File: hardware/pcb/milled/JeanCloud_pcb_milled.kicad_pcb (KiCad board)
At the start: 2 copper layers, 65 x 49 mm, 9 parts, among them J1 10118193-0001LF, U1 ESP32_DevKit_V1_DOIT

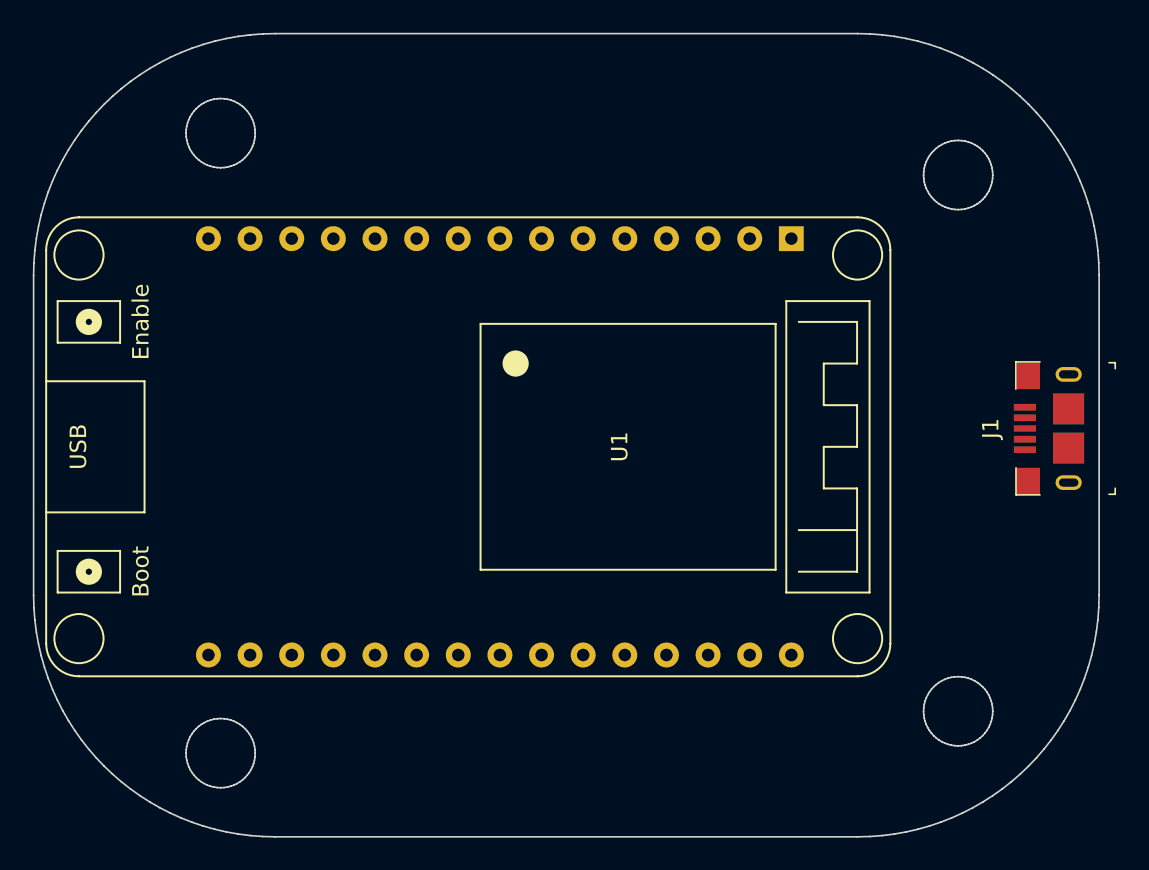
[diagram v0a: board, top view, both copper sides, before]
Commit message: finished pcb for milling
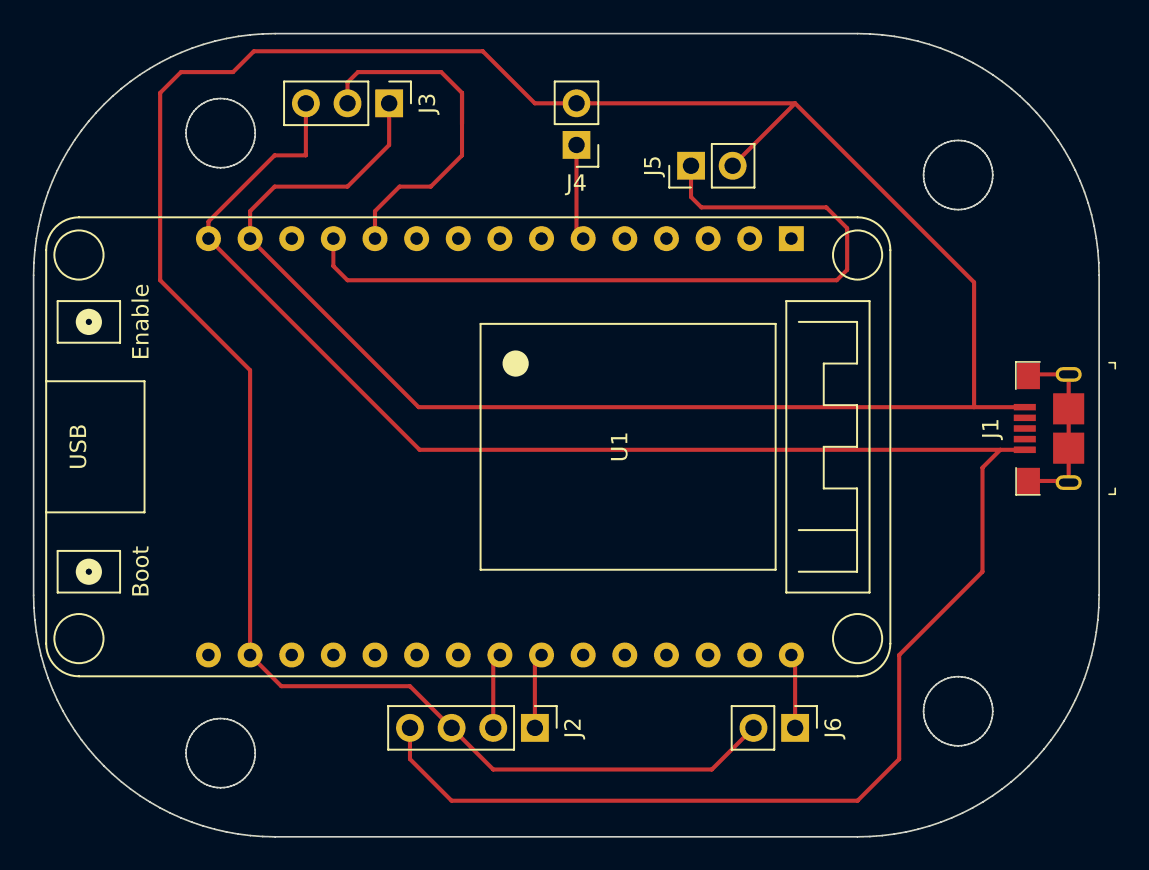
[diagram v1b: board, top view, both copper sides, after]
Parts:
- removed the G*** at (0.00, 0.00) (x7)
- added G*** (x7): LOGO, LOGO, F.Cu at (0.00, 0.00)
- added J2: Conn_01x04_Male, Connector_PinHeader_2.54mm:PinHeader_1x04_P2.54mm_Vertical, F.Cu at (67.3, 69.2)
- added J3: Conn_01x03_Male, Connector_PinHeader_2.54mm:PinHeader_1x03_P2.54mm_Vertical, F.Cu at (58.4, 31.1)
- added J4: Conn_01x02_Male, Connector_PinHeader_2.54mm:PinHeader_1x02_P2.54mm_Vertical, F.Cu at (69.8, 33.7)
- added J5: Conn_01x02_Male, Connector_PinHeader_2.54mm:PinHeader_1x02_P2.54mm_Vertical, F.Cu at (76.8, 34.9)
- added J6: Conn_01x02_Male, Connector_PinHeader_2.54mm:PinHeader_1x02_P2.54mm_Vertical, F.Cu at (83.2, 69.2)
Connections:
- U1 pad 14: Net-(U1-Pad14) -> GND
- U1 pad 15: Net-(U1-Pad15) -> 5V
- U1 pad 17: Net-(U1-Pad17) -> GND
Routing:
- net GND: track 0.00 -> 206.7 mm
- net 5V: track 0.00 -> 122.2 mm
- net Net-(J5-Pad1): track 0.00 -> 48.4 mm
- net Net-(J3-Pad2): track 0.00 -> 23.2 mm
- net Net-(J1-PadSH): track 0.00 -> 11.6 mm
- net Net-(J4-Pad1): track 0.00 -> 5.88 mm
- net Net-(J2-Pad2): track 0.00 -> 4.61 mm
- net Net-(J2-Pad1): track 0.00 -> 4.61 mm
- net Net-(J6-Pad1): track 0.00 -> 4.54 mm
